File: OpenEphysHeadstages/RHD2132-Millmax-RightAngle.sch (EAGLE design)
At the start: 16 parts, among them U1 RHD2132_QFN

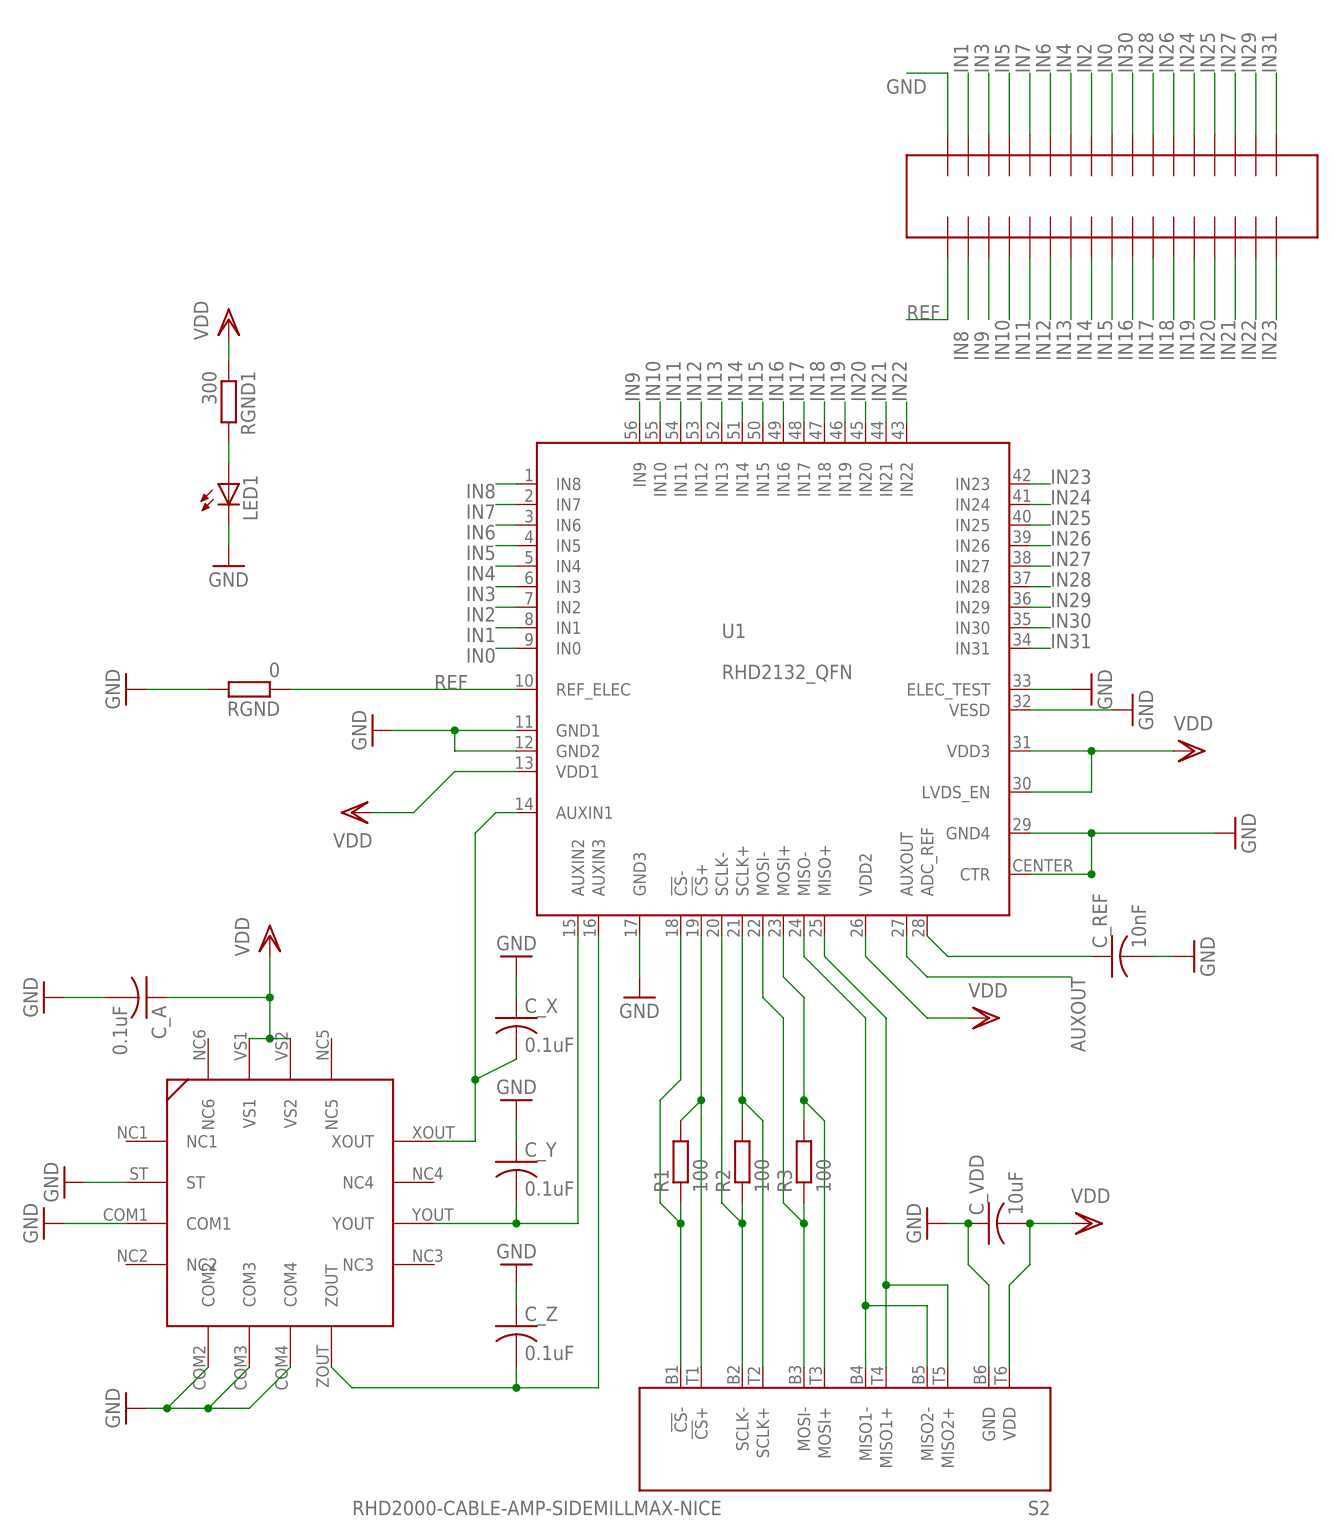
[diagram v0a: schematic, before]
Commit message: Updated solder paste to be little squares for center pads.
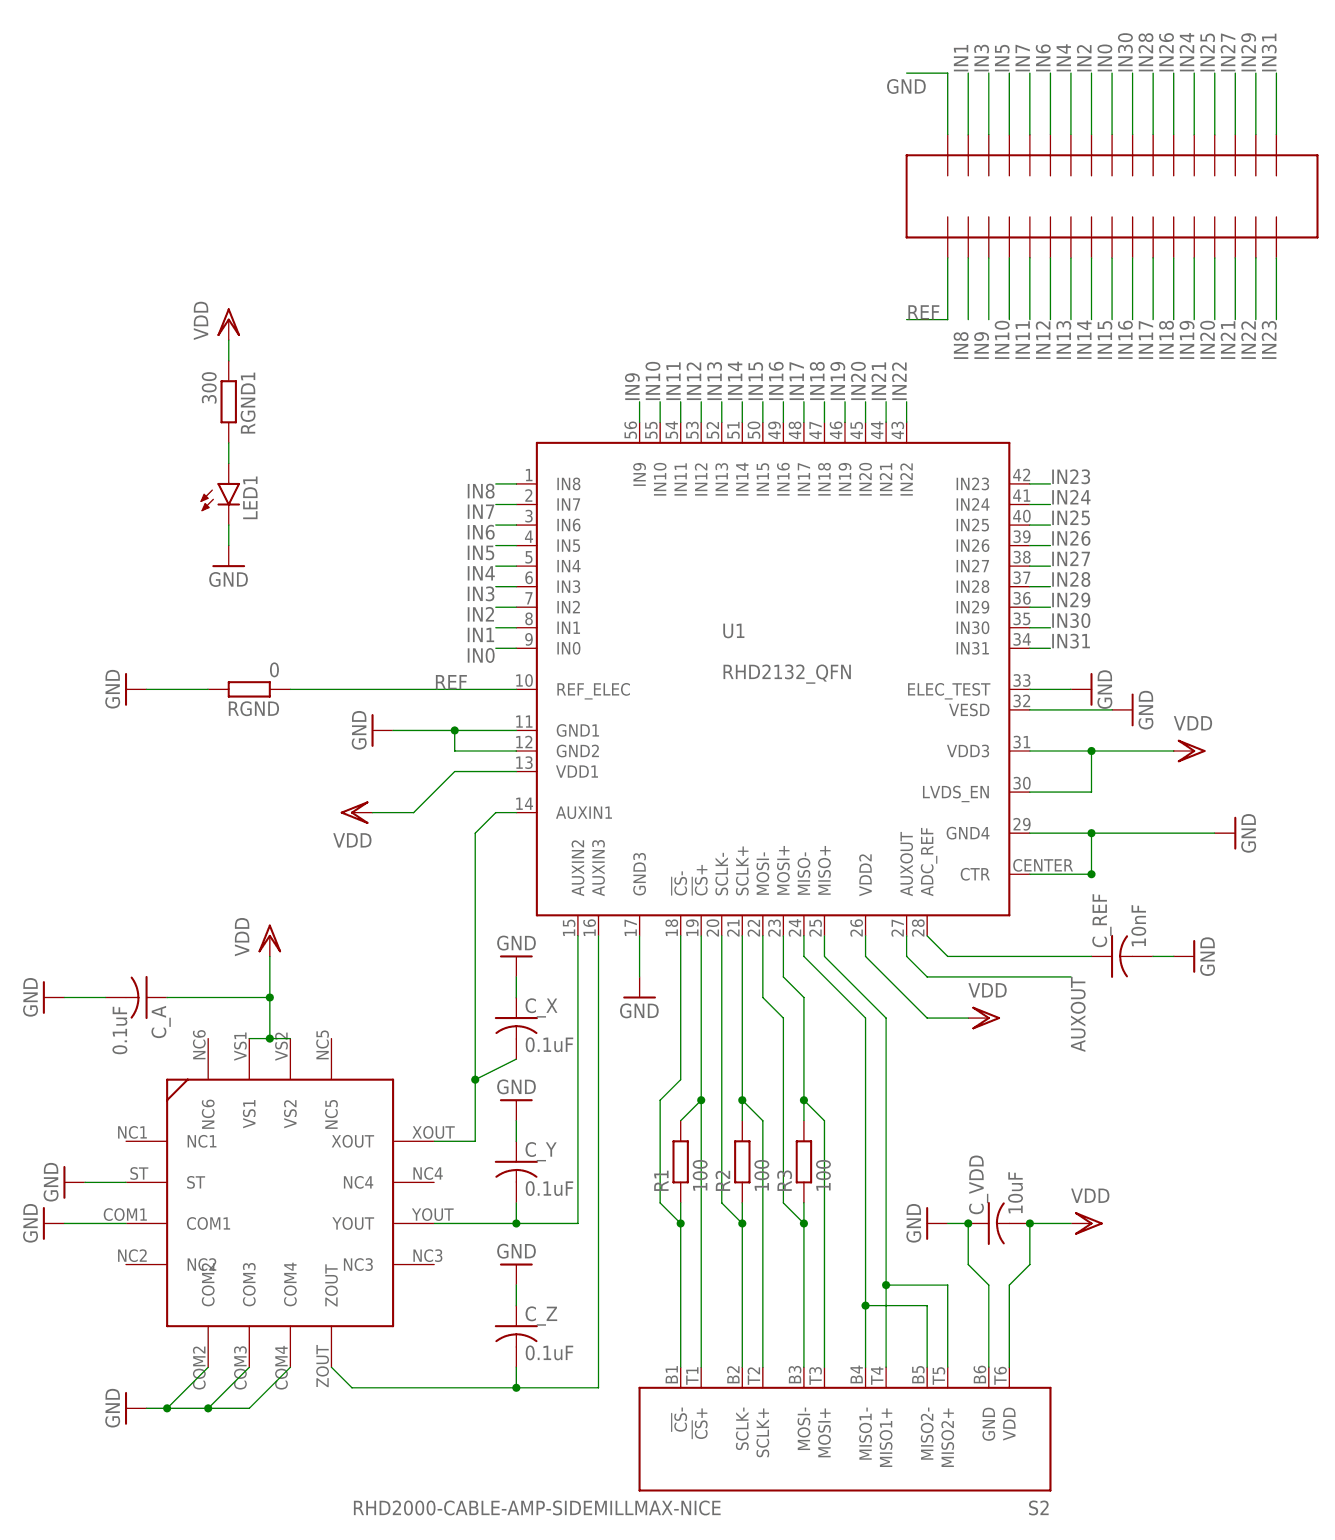
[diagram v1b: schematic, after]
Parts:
- S2: device RHD2000:RHD2000-CABLE-AMP-SIDEMILLMAX-NICE -> RHD2132-Millmax-RightAngle:RHD2000-CABLE-AMP-SIDEMILLMAX-NICE
- U$1: device voigts:ADXL335 -> RHD2132-Millmax-RightAngle:ADXL335
